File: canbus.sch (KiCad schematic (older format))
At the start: 8 parts

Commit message: Added more connection - incomplete
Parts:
- added R?: 1k, symbol R
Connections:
- net GND: now also R?.2
- net INT: now reaches U?.13 (~INT)
- net SCK: now reaches U?.14 (SCK)
- net SI: now reaches U?.16 (SI)
- net SO: now reaches U?.17 (SO)
- net CS: now reaches U?.18 (~CS)
- net at U?.19 (~RESET): now also R?.1
- no-connect marks 2 -> 8
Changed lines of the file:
@@
 Wire Wire Line
 	3450 3800 3450 4050
+NoConn ~ 3850 3550
+$Comp
+L R R?
+U 1 1 59E49315
+P 5150 4000
+F 0 "R?" V 5230 4000 50  0000 C CNN
+F 1 "1k" V 5150 4000 50  0000 C CNN
+F 2 "" V 5080 4000 50  0001 C CNN
+F 3 "" H 5150 4000 50  0001 C CNN
+	1    5150 4000
+	1    0    0    -1
+$EndComp
+Wire Wire Line
+	5050 3750 5150 3750
+Wire Wire Line
+	5150 3750 5150 3850
+$Comp
+L GND #PWR?
+U 1 1 59E4A43B
+P 5150 4450
+F 0 "#PWR?" H 5150 4200 50  0001 C CNN
+F 1 "GND" H 5150 4300 50  0000 C CNN
+F 2 "" H 5150 4450 50  0001 C CNN
+F 3 "" H 5150 4450 50  0001 C CNN
+	1    5150 4450
+	1    0    0    -1
+$EndComp
+Wire Wire Line
+	5150 4450 5150 4150
+Text Label 5350 3150 2    60   ~ 0
+INT
+Wire Wire Line
+	5050 3150 5350 3150
+NoConn ~ 5050 3650
+NoConn ~ 5050 3550
+NoConn ~ 5050 3450
+NoConn ~ 5050 3350
+NoConn ~ 5050 3250
+Text Label 3550 2550 0    60   ~ 0
+SI
+Text Label 3550 2650 0    60   ~ 0
+SO
+Text Label 3550 2750 0    60   ~ 0
+CS
+Text Label 3550 2850 0    60   ~ 0
+SCK
+Wire Wire Line
+	3550 2850 3850 2850
+Wire Wire Line
+	3850 2750 3550 2750
+Wire Wire Line
+	3550 2650 3850 2650
+Wire Wire Line
+	3850 2550 3550 2550
 $EndSCHEMATC

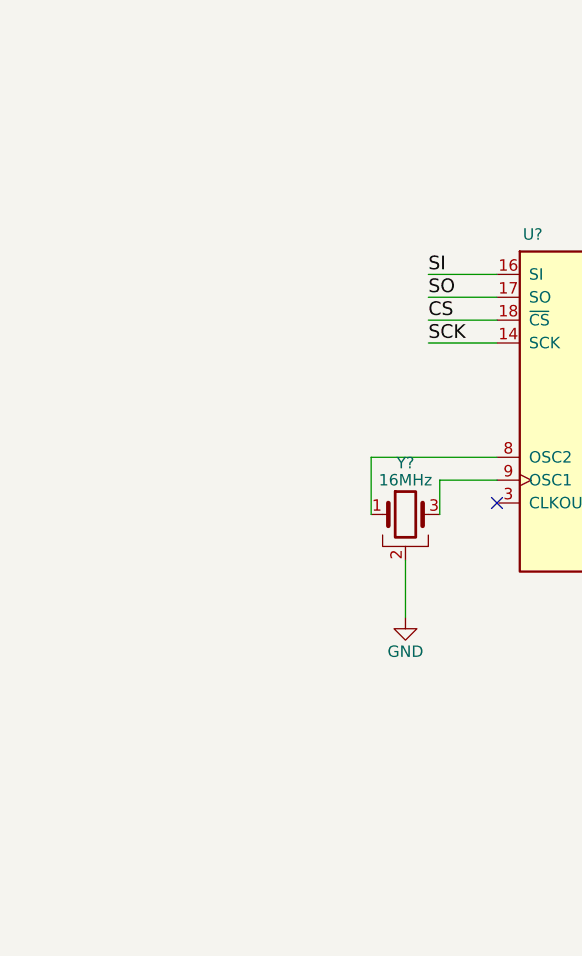
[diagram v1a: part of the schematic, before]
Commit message: Started vref selector and main connector pins
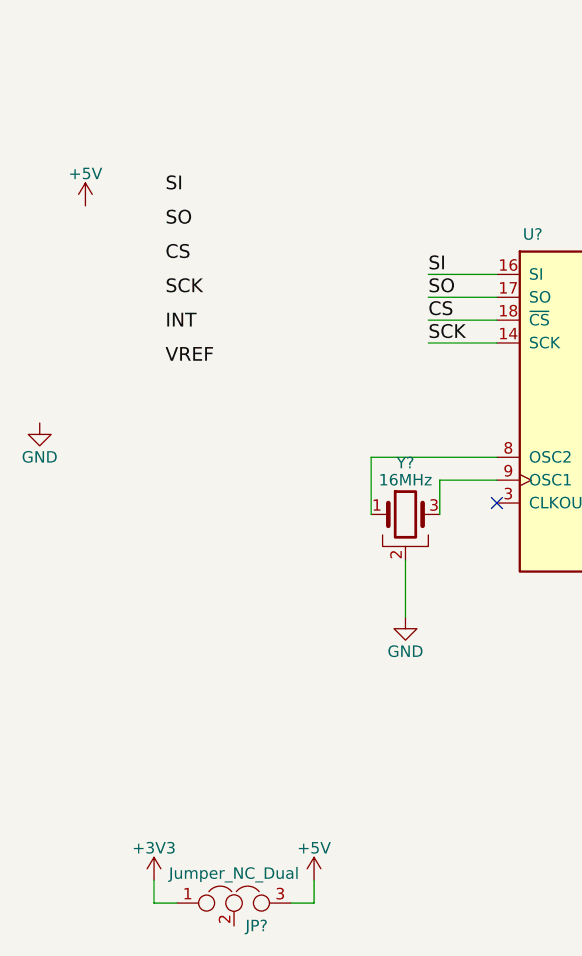
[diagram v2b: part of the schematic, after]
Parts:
- added JP?: Jumper_NC_Dual, symbol Jumper_NC_Dual
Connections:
- net +5V: now also JP?.3
- new net +3V3: JP?.1
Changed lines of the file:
@@
 LIBS:contrib
 LIBS:valves
+LIBS:canbus-cache
 EELAYER 25 0
 EELAYER END
@@
 Wire Wire Line
 	3850 2550 3550 2550
+Text Label 2400 2200 0    60   ~ 0
+SI
+Text Label 2400 2350 0    60   ~ 0
+SO
+Text Label 2400 2500 0    60   ~ 0
+CS
+Text Label 2400 2650 0    60   ~ 0
+SCK
+Text Label 2400 2800 0    60   ~ 0
+INT
+Text Label 2400 2950 0    60   ~ 0
+VREF
+$Comp
+L +5V #PWR?
+U 1 1 59E4D6B5
+P 2050 2250
+F 0 "#PWR?" H 2050 2100 50  0001 C CNN
+F 1 "+5V" H 2050 2390 50  0000 C CNN
+F 2 "" H 2050 2250 50  0001 C CNN
+F 3 "" H 2050 2250 50  0001 C CNN
+	1    2050 2250
+	1    0    0    -1
+$EndComp
+$Comp
+L GND #PWR?
+U 1 1 59E4D6DB
+P 1850 3200
+F 0 "#PWR?" H 1850 2950 50  0001 C CNN
+F 1 "GND" H 1850 3050 50  0000 C CNN
+F 2 "" H 1850 3200 50  0001 C CNN
+F 3 "" H 1850 3200 50  0001 C CNN
+	1    1850 3200
+	1    0    0    -1
+$EndComp
+$Comp
+L Jumper_NC_Dual JP?
+U 1 1 59E4DDBA
+P 2700 5300
+F 0 "JP?" H 2750 5200 50  0000 L CNN
+F 1 "Jumper_NC_Dual" H 2700 5400 50  0000 C BNN
+F 2 "" H 2700 5300 50  0001 C CNN
+F 3 "" H 2700 5300 50  0001 C CNN
+	1    2700 5300
+	1    0    0    -1
+$EndComp
+$Comp
+L +5V #PWR?
+U 1 1 59E4DFD1
+P 3050 5200
+F 0 "#PWR?" H 3050 5050 50  0001 C CNN
+F 1 "+5V" H 3050 5340 50  0000 C CNN
+F 2 "" H 3050 5200 50  0001 C CNN
+F 3 "" H 3050 5200 50  0001 C CNN
+	1    3050 5200
+	1    0    0    -1
+$EndComp
+$Comp
+L +3V3 #PWR?
+U 1 1 59E4DFF9
+P 2350 5200
+F 0 "#PWR?" H 2350 5050 50  0001 C CNN
+F 1 "+3V3" H 2350 5340 50  0000 C CNN
+F 2 "" H 2350 5200 50  0001 C CNN
+F 3 "" H 2350 5200 50  0001 C CNN
+	1    2350 5200
+	1    0    0    -1
+$EndComp
+Wire Wire Line
+	2350 5200 2350 5300
+Wire Wire Line
+	2350 5300 2450 5300
+Wire Wire Line
+	2950 5300 3050 5300
+Wire Wire Line
+	3050 5300 3050 5200
 $EndSCHEMATC

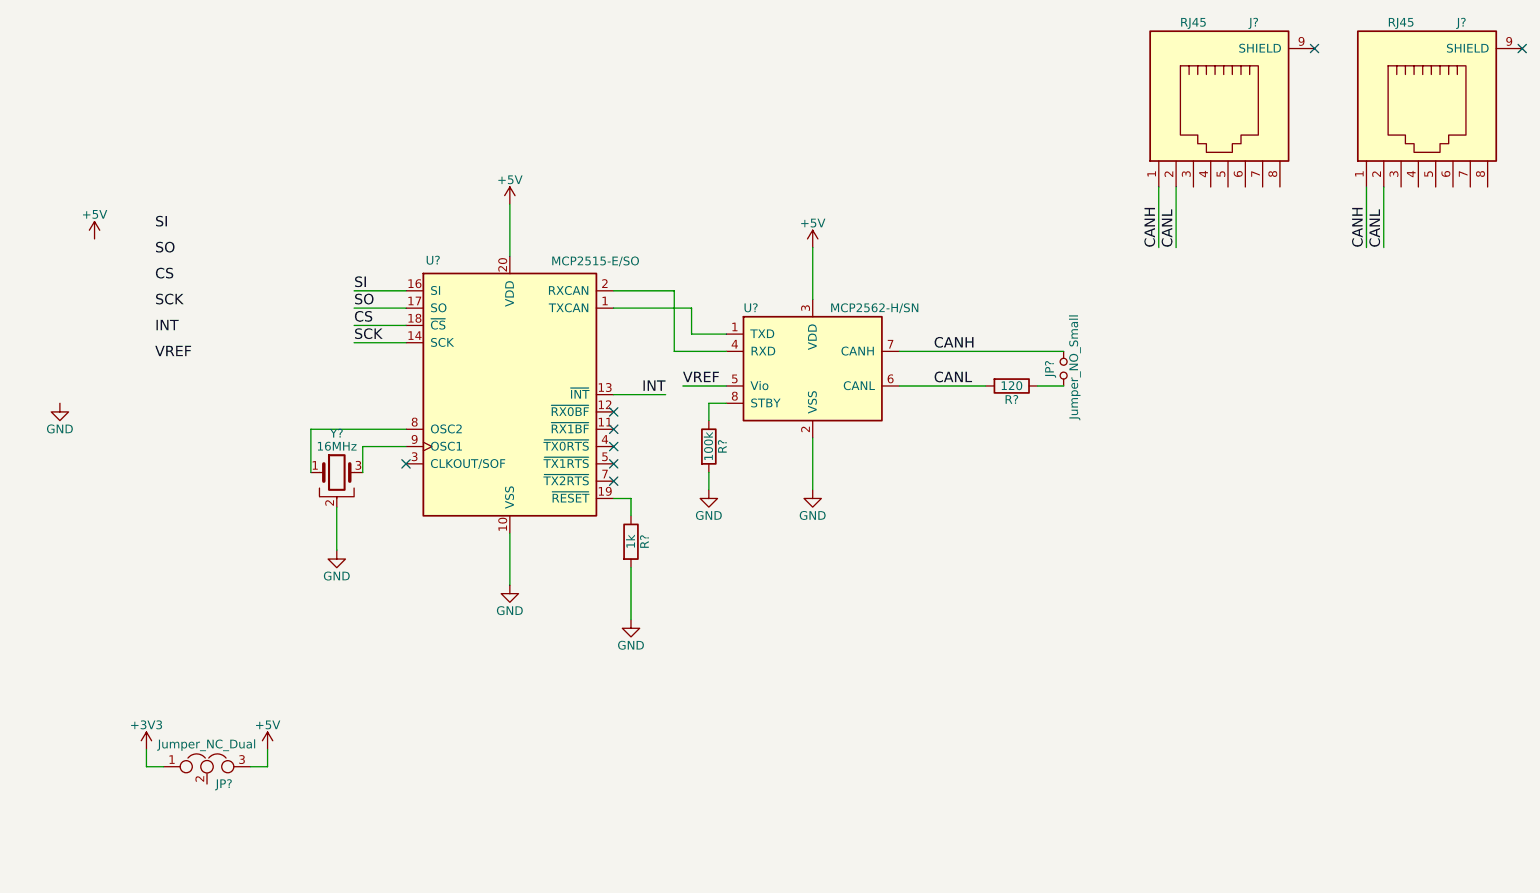
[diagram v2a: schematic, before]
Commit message: Finished schematic and component association
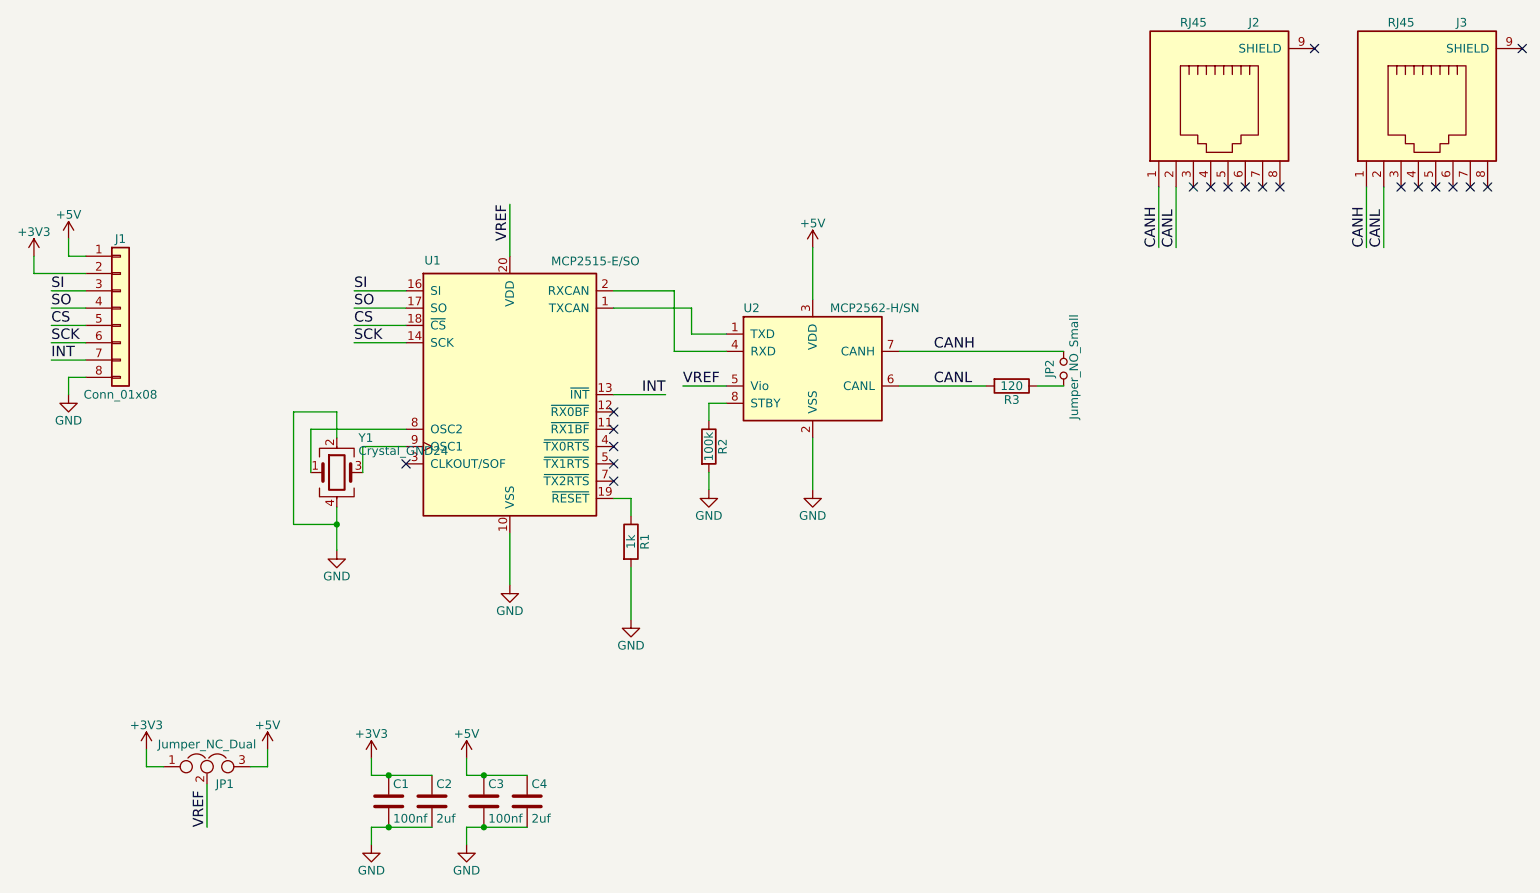
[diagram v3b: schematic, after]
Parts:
- removed Y?: 16MHz, symbol Crystal_GND2
- added C1, C3: 100nf, Capacitors_SMD:C_0805_HandSoldering, symbol C
- added C2, C4: 2uf, Capacitors_SMD:C_0805_HandSoldering, symbol C
- added J1: Conn_01x08, Pin_Headers:Pin_Header_Straight_1x08_Pitch2.54mm, symbol Conn_01x08
- added Y1: Crystal_GND24, Crystals:Crystal_SMD_5032-4pin_5.0x3.2mm, symbol Crystal_GND24
- J2, J3: renamed from J?; footprint (none) -> Connectors:RJ45_8
- JP1: renamed from JP?; footprint (none) -> Pin_Headers:Pin_Header_Straight_1x03_Pitch2.54mm
- JP2: renamed from JP?; footprint (none) -> Pin_Headers:Pin_Header_Straight_1x02_Pitch2.54mm
- R1, R2, R3: renamed from R?; footprint (none) -> Resistors_SMD:R_0805_HandSoldering
- gave numbers to parts that had none: 2
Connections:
- net +3V3: now also C1.1, C2.1, J1.2 (Pin_2)
- net +5V: now also C3.1, C4.1, J1.1 (Pin_1); no longer U1.20 (VDD)
- net CS: now also J1.5 (Pin_5)
- net GND: now also C1.2, C2.2, C3.2, C4.2, J1.8 (Pin_8), Y1.2, Y1.4
- net INT: now also J1.7 (Pin_7)
- net SCK: now also J1.6 (Pin_6)
- net SI: now also J1.3 (Pin_3)
- net SO: now also J1.4 (Pin_4)
- net VREF: now also JP1.2, U1.20 (VDD)
- net at U1.8 (OSC2): now also Y1.1
- net at U1.9 (OSC1): now also Y1.3
- no-connect marks 8 -> 20

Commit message: Changed MCP2515 to SOIC-18 - Unfinished
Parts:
- U1: footprint Housings_SSOP:TSSOP-20_4.4x6.5mm_Pitch0.65mm -> soic-18:SOIC-18
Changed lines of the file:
@@
 F 0 "U1" H 4050 3925 50  0000 R CNN
 F 1 "MCP2515-E/SO" H 5200 3950 50  0000 R TNN
-F 2 "Housings_SSOP:TSSOP-20_4.4x6.5mm_Pitch0.65mm" H 4450 2250 50  0001 C CIN
+F 2 "soic-18:SOIC-18" H 4450 2250 50  0001 C CIN
 F 3 "" H 4550 2350 50  0001 C CNN
 	1    4450 3150

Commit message: Corrected schematic mistakes and updated pcb to match
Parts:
- removed U1: MCP2515-E/SO, soic-18:SOIC-18, symbol MCP2515-E/ST
- added U1: MCP2515-E/SO, soic-18:SOIC-18, symbol MCP2515-E/SO
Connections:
- net CS: now also J1.3 (Pin_3), U1.16 (~CS); no longer J1.5 (Pin_5)
- net GND: now also U1.9 (VSS)
- net INT: now also U1.12 (~INT)
- net SCK: now also U1.13 (SCK)
- net SI: now also J1.5 (Pin_5), U1.14 (SI); no longer J1.3 (Pin_3)
- net SO: now also U1.15 (SO)
- net VREF: now also U1.18 (VDD)
- net at U2.1 (TXD): now also U1.1 (TXCAN)
- net at U2.4 (RXD): now also U1.2 (RXCAN)
- net at R1.1: now also U1.17 (~RESET)
- net at Y1.1: now also U1.7 (OSC2)
- net at Y1.3: now also U1.8 (OSC1)
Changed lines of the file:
@@
 LIBS:contrib
 LIBS:valves
+LIBS:MCP2515-E.SO
 LIBS:canbus-cache
 EELAYER 25 0
@@
 $EndComp
 $Comp
-L MCP2515-E/ST U1
-U 1 1 59E4354F
-P 4450 3150
-F 0 "U1" H 4050 3925 50  0000 R CNN
-F 1 "MCP2515-E/SO" H 5200 3950 50  0000 R TNN
-F 2 "soic-18:SOIC-18" H 4450 2250 50  0001 C CIN
-F 3 "" H 4550 2350 50  0001 C CNN
-	1    4450 3150
-	1    0    0    -1
-$EndComp
-$Comp
 L RJ45 J2
 U 1 1 59E43703
@@
 Text Label 3550 2850 0    60   ~ 0
 SCK
-Text Label 1800 2550 0    60   ~ 0
+Text Label 1800 2750 0    60   ~ 0
 SI
 Text Label 1800 2650 0    60   ~ 0
 SO
-Text Label 1800 2750 0    60   ~ 0
+Text Label 1800 2550 0    60   ~ 0
 CS
 Text Label 1800 2850 0    60   ~ 0
@@
 NoConn ~ 10000 1950
 NoConn ~ 10100 1950
+$Comp
+L MCP2515-E/SO U1
+U 1 1 59FB61DC
+P 4450 3150
+F 0 "U1" H 4050 3925 50  0000 R CNN
+F 1 "MCP2515-E/SO" H 5200 3950 50  0000 R TNN
+F 2 "soic-18:SOIC-18" H 4450 2250 50  0001 C CIN
+F 3 "" H 4550 2350 50  0001 C CNN
+	1    4450 3150
+	1    0    0    -1
+$EndComp
 $EndSCHEMATC

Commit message: Changed SOIC18 footprint to builtin
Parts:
- U1: footprint soic-18:SOIC-18 -> Housings_SOIC:SOIC-18W_7.5x11.6mm_Pitch1.27mm
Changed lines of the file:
@@
 F 0 "U1" H 4050 3925 50  0000 R CNN
 F 1 "MCP2515-E/SO" H 5200 3950 50  0000 R TNN
-F 2 "soic-18:SOIC-18" H 4450 2250 50  0001 C CIN
+F 2 "Housings_SOIC:SOIC-18W_7.5x11.6mm_Pitch1.27mm" H 4450 2250 50  0001 C CIN
 F 3 "" H 4550 2350 50  0001 C CNN
 	1    4450 3150
